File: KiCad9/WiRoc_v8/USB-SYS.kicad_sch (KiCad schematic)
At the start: 20 parts, among them U13 SGM803-RXN3L, Y2 24MHz/18pF

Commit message: etc
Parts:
- C36: LCSC Part # (none) -> C52923; Manufacturer (none) -> Samsung Electro-Mechanics; ManufacturerPartNumber (none) -> CL05A105KA5NQNC
- C38, C44: LCSC Part # (none) -> C23733; Manufacturer (none) -> Samsung Electro-Mechanics; ManufacturerPartNumber (none) -> CL05A475MP5NRNC
- R29, R30, R31, R32: LCSC Part # (none) -> C25804; Manufacturer (none) -> Uniroyal Elec; ManufacturerPartNumber (none) -> 0603WAF1002T5E
- U11: value ~ -> AllwinnerH3
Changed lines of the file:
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@@
 			)
 		)
+		(property "LCSC Part #" "C23733"
+			(at 110.49 69.85 90)
+			(effects
+				(font
+					(size 1.27 1.27)
+				)
+				(hide yes)
+			)
+		)
+		(property "Manufacturer" "Samsung Electro-Mechanics"
+			(at 110.49 69.85 90)
+			(effects
+				(font
+					(size 1.27 1.27)
+				)
+				(hide yes)
+			)
+		)
+		(property "ManufacturerPartNumber" "CL05A475MP5NRNC"
+			(at 110.49 69.85 90)
+			(effects
+				(font
+					(size 1.27 1.27)
+				)
+				(hide yes)
+			)
+		)
 		(pin "1"
 		)
@@
 			)
 		)
-		(property "Value" "~"
+		(property "Value" "AllwinnerH3"
 			(at 227.33 74.93 0)
 			(effects
@@
 			)
 		)
-		(property "Datasheet" "~"
+		(property "Datasheet" "https://jlcpcb.com/api/file/downloadByFileSystemAccessId/8579707174974914560"
 			(at 193.04 55.88 0)
 			(effects
@@
 			)
 		)
+		(property "LCSC Part #" "C52923"
+			(at 193.04 55.88 90)
+			(effects
+				(font
+					(size 1.27 1.27)
+				)
+				(hide yes)
+			)
+		)
+		(property "Manufacturer" "Samsung Electro-Mechanics"
+			(at 193.04 55.88 90)
+			(effects
+				(font
+					(size 1.27 1.27)
+				)
+				(hide yes)
+			)
+		)
+		(property "ManufacturerPartNumber" "CL05A105KA5NQNC"
+			(at 193.04 55.88 90)
+			(effects
+				(font
+					(size 1.27 1.27)
+				)
+				(hide yes)
+			)
+		)
 		(pin "1"
 		)
@@
 			)
 		)
+		(property "LCSC Part #" "C25804"
+			(at 81.28 165.1 90)
+			(effects
+				(font
+					(size 1.27 1.27)
+				)
+				(hide yes)
+			)
+		)
+		(property "Manufacturer" "Uniroyal Elec"
+			(at 81.28 165.1 90)
+			(effects
+				(font
+					(size 1.27 1.27)
+				)
+				(hide yes)
+			)
+		)
+		(property "ManufacturerPartNumber" "0603WAF1002T5E"
+			(at 81.28 165.1 90)
+			(effects
+				(font
+					(size 1.27 1.27)
+				)
+				(hide yes)
+			)
+		)
 		(pin "1"
 		)
@@
 			)
 		)
+		(property "LCSC Part #" "C25804"
+			(at 81.28 167.64 90)
+			(effects
+				(font
+					(size 1.27 1.27)
+				)
+				(hide yes)
+			)
+		)
+		(property "Manufacturer" "Uniroyal Elec"
+			(at 81.28 167.64 90)
+			(effects
+				(font
+					(size 1.27 1.27)
+				)
+				(hide yes)
+			)
+		)
+		(property "ManufacturerPartNumber" "0603WAF1002T5E"
+			(at 81.28 167.64 90)
+			(effects
+				(font
+					(size 1.27 1.27)
+				)
+				(hide yes)
+			)
+		)
 		(pin "1"
 		)
@@
 			)
 		)
+		(property "LCSC Part #" "C25804"
+			(at 160.02 121.92 90)
+			(effects
+				(font
+					(size 1.27 1.27)
+				)
+				(hide yes)
+			)
+		)
+		(property "Manufacturer" "Uniroyal Elec"
+			(at 160.02 121.92 90)
+			(effects
+				(font
+					(size 1.27 1.27)
+				)
+				(hide yes)
+			)
+		)
+		(property "ManufacturerPartNumber" "0603WAF1002T5E"
+			(at 160.02 121.92 90)
+			(effects
+				(font
+					(size 1.27 1.27)
+				)
+				(hide yes)
+			)
+		)
 		(pin "1"
 		)
@@
 			)
 		)
+		(property "LCSC Part #" "C23733"
+			(at 130.81 91.44 90)
+			(effects
+				(font
+					(size 1.27 1.27)
+				)
+				(hide yes)
+			)
+		)
+		(property "Manufacturer" "Samsung Electro-Mechanics"
+			(at 130.81 91.44 90)
+			(effects
+				(font
+					(size 1.27 1.27)
+				)
+				(hide yes)
+			)
+		)
+		(property "ManufacturerPartNumber" "CL05A475MP5NRNC"
+			(at 130.81 91.44 90)
+			(effects
+				(font
+					(size 1.27 1.27)
+				)
+				(hide yes)
+			)
+		)
 		(pin "1"
 		)
@@
 			)
 		)
-		(property "Value" "~"
+		(property "Value" "AllwinnerH3"
 			(at 49.53 59.69 0)
 			(effects
@@
 			)
 		)
-		(property "Value" "~"
+		(property "Value" "AllwinnerH3"
 			(at 50.8 173.99 0)
 			(effects
@@
 			(effects
 				(font
+					(size 1.27 1.27)
+				)
+				(hide yes)
+			)
+		)
+		(property "LCSC Part #" "C25804"
+			(at 130.81 43.18 90)
+			(effects
+				(font
+					(size 1.27 1.27)
+				)
+				(hide yes)
+			)
+		)
+		(property "Manufacturer" "Uniroyal Elec"
+			(at 130.81 43.18 90)
+			(effects
+				(font
+					(size 1.27 1.27)
+				)
+				(hide yes)
+			)
+		)
+		(property "ManufacturerPartNumber" "0603WAF1002T5E"
+			(at 130.81 43.18 90)
+			(effects
+				(font

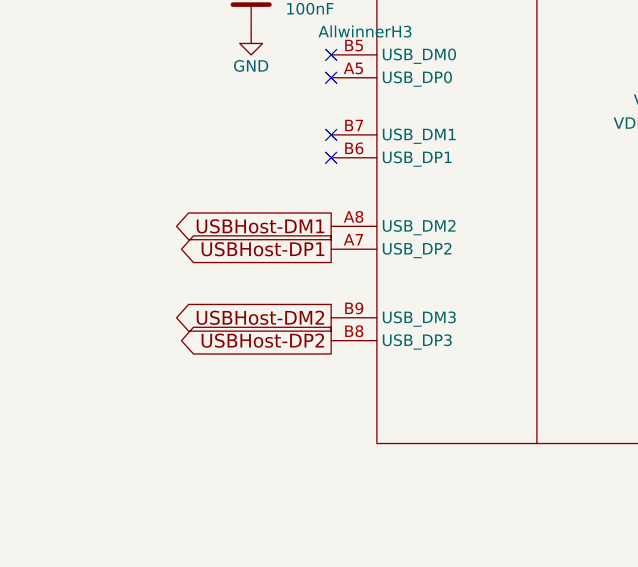
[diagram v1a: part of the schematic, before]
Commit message: more routing of WiRoc_v8, upgraded USBConnectorPlate to v9 and with ferrit beads, added an ESPHosted testboard
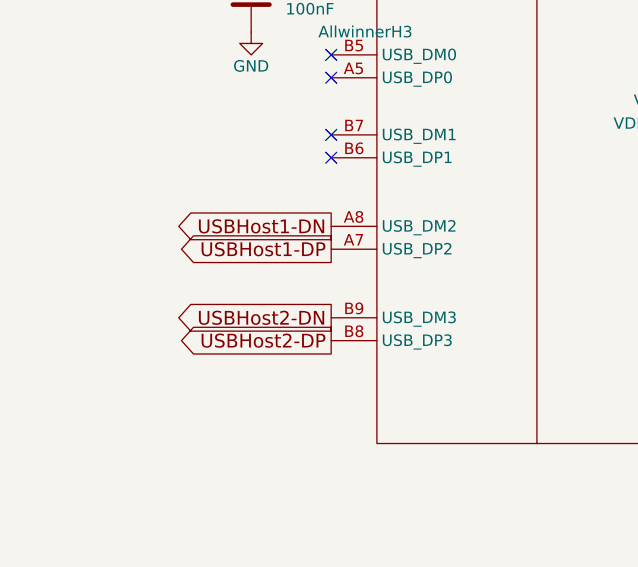
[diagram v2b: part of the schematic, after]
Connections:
- net USBHost-DM1 renamed USBHost1-DN
- net USBHost-DM2 renamed USBHost2-DN
- net USBHost-DP1 renamed USBHost1-DP
- net USBHost-DP2 renamed USBHost2-DP
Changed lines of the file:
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@@
 		)
 	)
-	(global_label "USBHost-DM1"
+	(global_label "USBHost1-DN"
 		(shape output)
 		(at 45.72 81.28 180)
@@
 		)
 		(property "Intersheetrefs" "${INTERSHEET_REFS}"
-			(at 26.6671 81.28 0)
+			(at 26.8122 81.28 0)
 			(effects
 				(font
@@
 		)
 	)
-	(global_label "USBHost-DP1"
+	(global_label "USBHost1-DP"
 		(shape output)
 		(at 45.72 83.82 180)
@@
 		)
 	)
-	(global_label "USBHost-DM2"
+	(global_label "USBHost2-DN"
 		(shape output)
 		(at 45.72 91.44 180)
@@
 		)
 		(property "Intersheetrefs" "${INTERSHEET_REFS}"
-			(at 26.6671 91.44 0)
+			(at 26.8122 91.44 0)
 			(effects
 				(font
@@
 		)
 	)
-	(global_label "USBHost-DP2"
+	(global_label "USBHost2-DP"
 		(shape output)
 		(at 45.72 93.98 180)

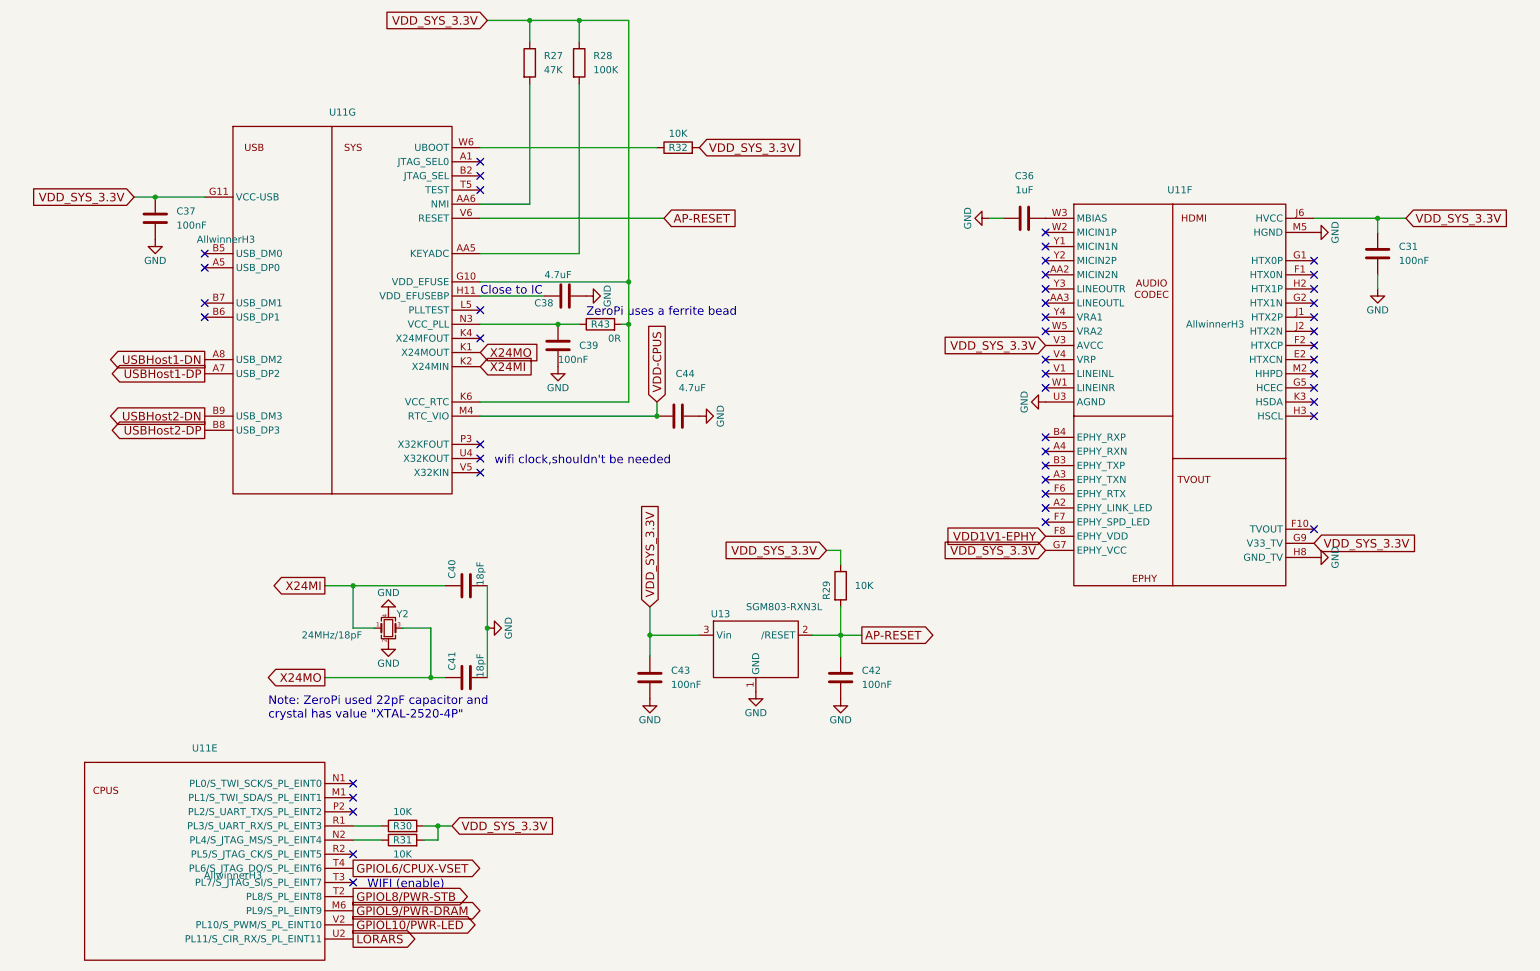
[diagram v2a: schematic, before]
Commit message: add bom
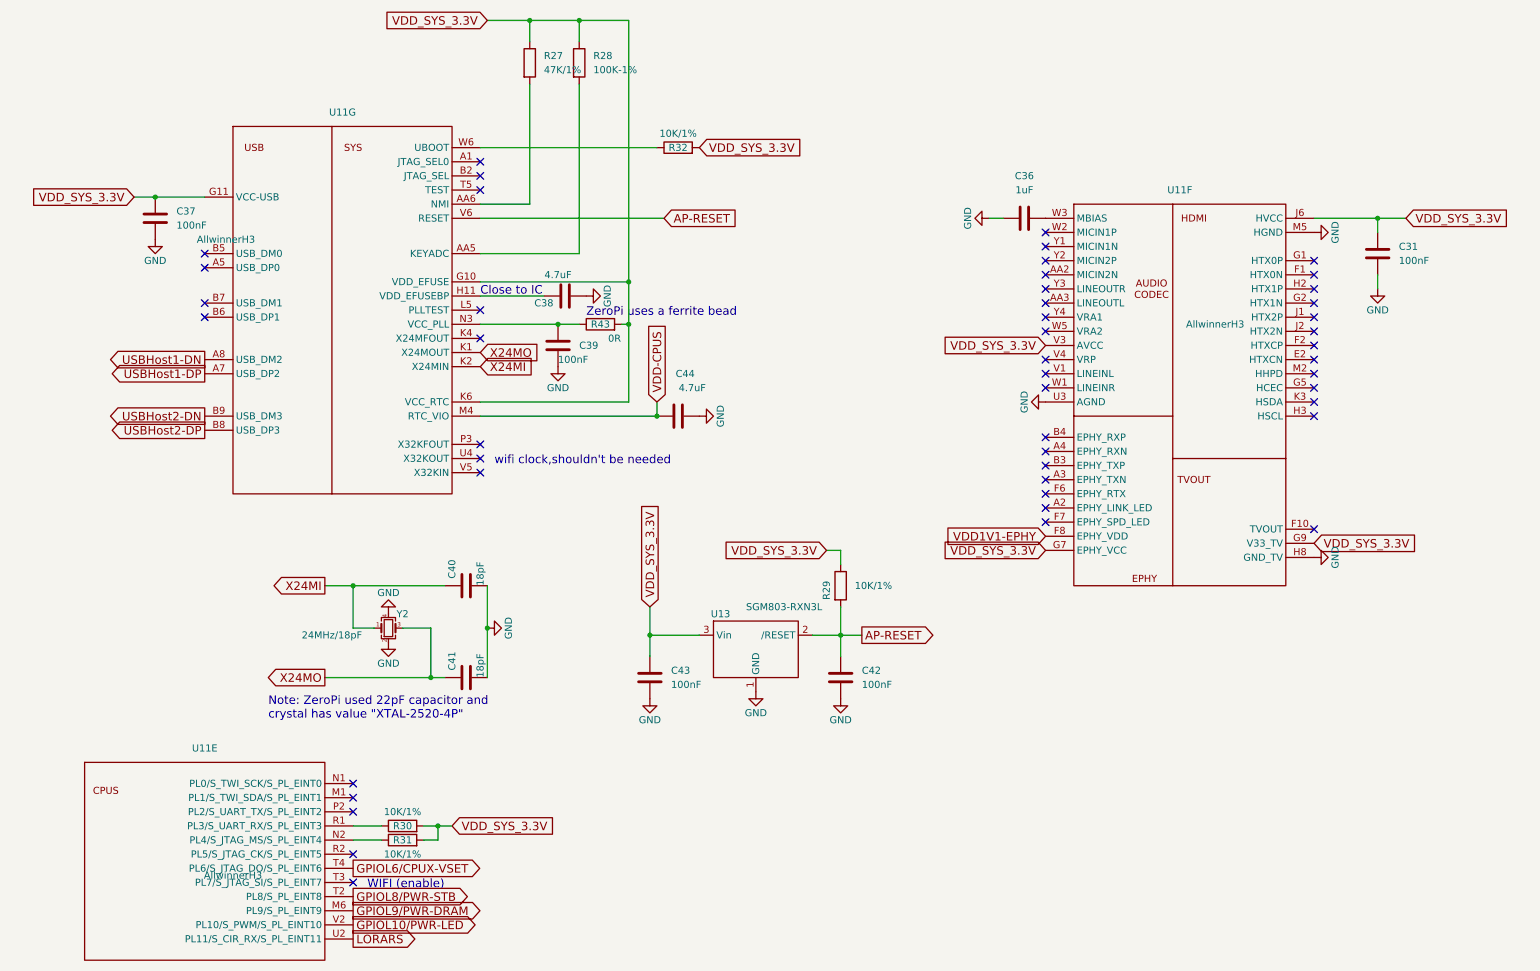
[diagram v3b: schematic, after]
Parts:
- C31, C37, C39, C42, C43: IncludeInBOM (none) -> TRUE; JLCBasicExtended (none) -> Basic; LCSC Part # (none) -> C1525; Manufacturer (none) -> Samsung Electro-Mechanics; ManufacturerPartNumber (none) -> CL05B104KO5NNNC; Package (none) -> 0402
- C36, C38, C44: IncludeInBOM (none) -> TRUE; JLCBasicExtended (none) -> Basic; Package (none) -> 0402
- C40, C41: IncludeInBOM (none) -> TRUE; JLCBasicExtended (none) -> Basic; LCSC Part # (none) -> C1549; Manufacturer (none) -> FH (Guangdong Fenghua Advanced Tech); ManufacturerPartNumber (none) -> 0402CG180J500NT; Package (none) -> 0402
- R27: value 47K -> 47K/1%; IncludeInBOM (none) -> TRUE; JLCBasicExtended (none) -> Basic; LCSC Part # (none) -> C25792; Manufacturer (none) -> Uniroyal Elec; ManufacturerPartNumber (none) -> 0402WGF4702TCE; Package (none) -> 0402
- R28: value 100K -> 100K-1%; IncludeInBOM (none) -> TRUE; JLCBasicExtended (none) -> Basic; LCSC Part # (none) -> C25741; Manufacturer (none) -> Uniroyal Elec; ManufacturerPartNumber (none) -> 0402WGF1003TCE; Package (none) -> 0402
- R29, R30, R31, R32: value 10K -> 10K/1%; IncludeInBOM (none) -> TRUE; JLCBasicExtended (none) -> Basic; LCSC Part # C25804 -> C25744; ManufacturerPartNumber 0603WAF1002T5E -> 0402WGF1002TCE; Package (none) -> 0402
- R43: IncludeInBOM (none) -> TRUE; JLCBasicExtended (none) -> Basic; LCSC Part # (none) -> C17168; Manufacturer (none) -> Uniroyal Elec; ManufacturerPartNumber (none) -> 0402WGF0000TCE; Package (none) -> 0402
- U11: IncludeInBOM (none) -> TRUE; JLCBasicExtended (none) -> Extended; LCSC Part # (none) -> C94644; Manufacturer (none) -> Allwinner; ManufacturerPartNumber (none) -> H3; Package (none) -> FBGA-347(14x14)
- U13: IncludeInBOM (none) -> TRUE; JLCBasicExtended (none) -> Extended; LCSC Part # (none) -> C5152590; Manufacturer (none) -> SGMICRO; ManufacturerPartNumber (none) -> SGM803-RXN3L/TR; Package (none) -> SOT-23
- Y2: IncludeInBOM (none) -> TRUE; JLCBasicExtended (none) -> Extended; LCSC Part # (none) -> C284161; Manufacturer (none) -> Yajingxin; ManufacturerPartNumber (none) -> TXM24M0004252FBCEO00T; Package (none) -> SMD2520-4P

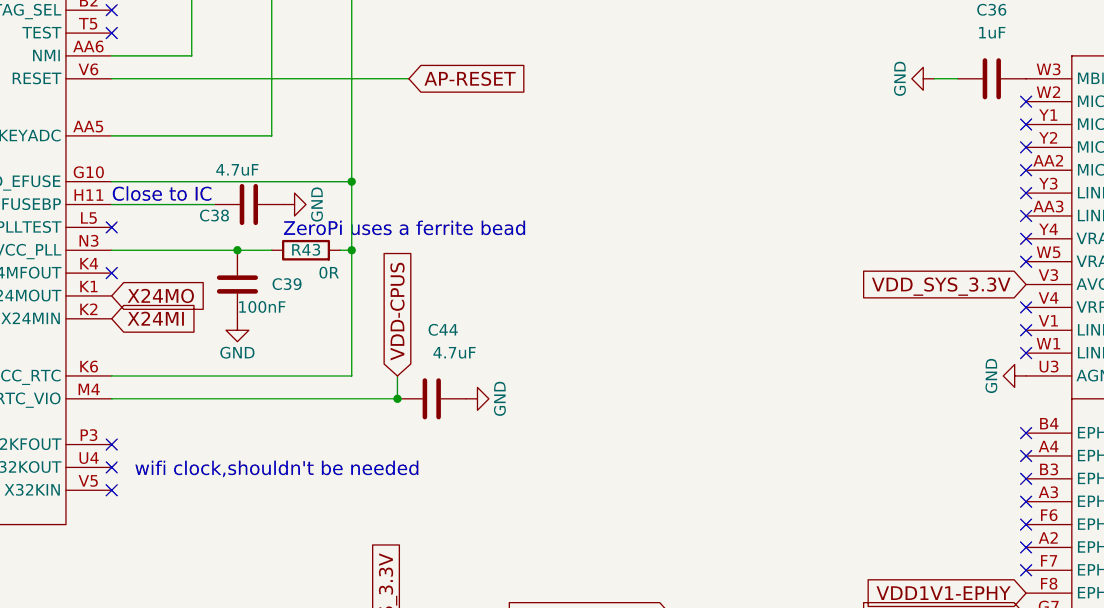
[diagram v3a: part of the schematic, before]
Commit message: add esp32hosted-c5 board
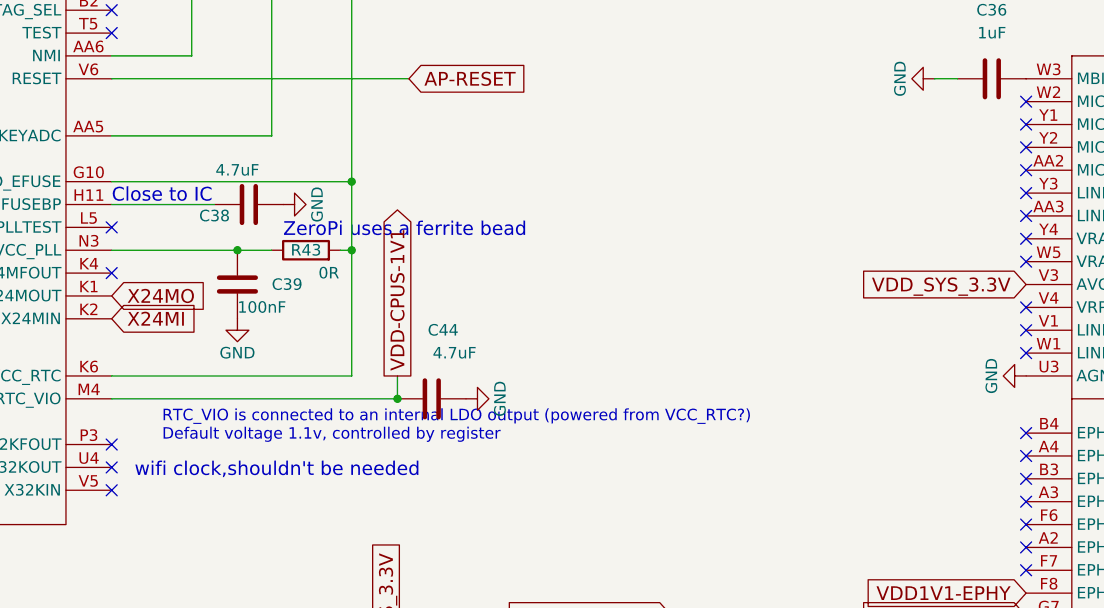
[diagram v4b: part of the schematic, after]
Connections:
- net VDD-CPUS renamed VDD-CPUS-1V1
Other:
- note added: "RTC_VIO is connected to an internal LDO output (powered from VCC_RTC?) Default voltage 1.1v, controlled by register"
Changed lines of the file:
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@@
+		)
+	)
+	(text "RTC_VIO is connected to an internal LDO output (powered from VCC_RTC?)\nDefault voltage 1.1v, controlled by register"
+		(exclude_from_sim no)
+		(at 100.838 96.266 0)
+		(effects
+			(font
+				(size 1.27 1.27)
+			)
+			(justify left bottom)
 		)
 	)
@@
 		)
 	)
-	(global_label "VDD-CPUS"
-		(shape input)
+	(global_label "VDD-CPUS-1V1"
+		(shape output)
 		(at 127 88.9 90)
 		(fields_autoplaced yes)
@@
 		)
 		(property "Intersheetrefs" "${INTERSHEET_REFS}"
-			(at 127 73.766 90)
-			(effects
-				(font
+			(at 127 67.67 90)
+			(effects
+				(font
